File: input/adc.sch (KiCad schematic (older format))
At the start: 23 parts, among them J102 +IN, J103 -IN, U101 LTC2512-24

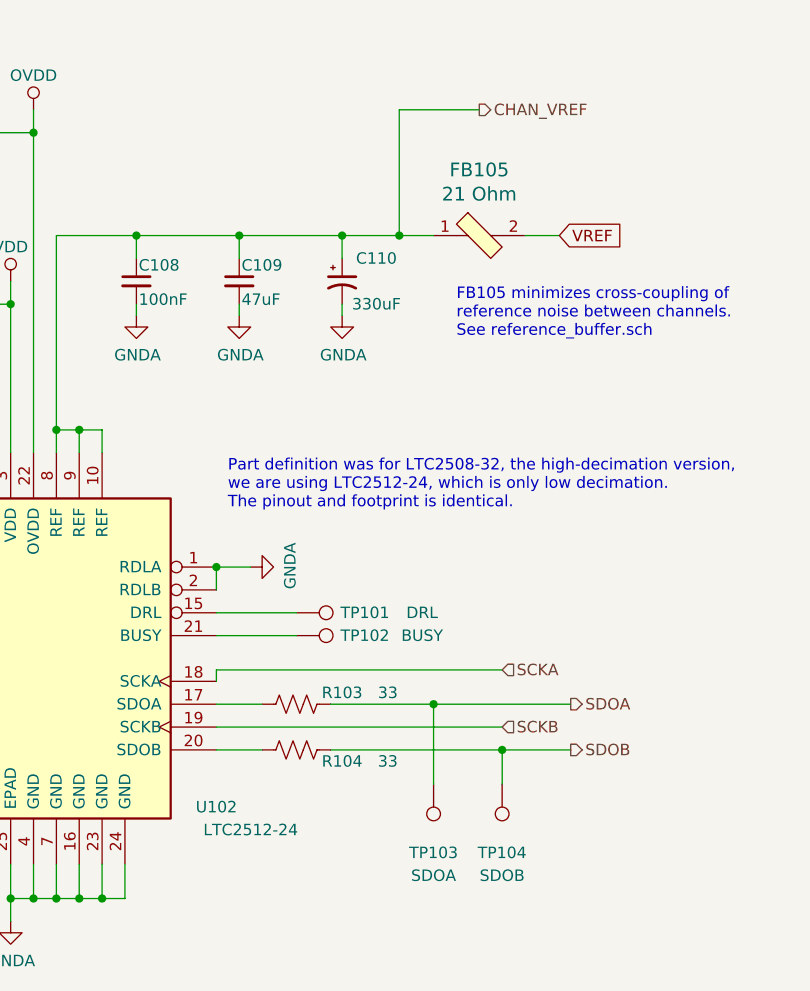
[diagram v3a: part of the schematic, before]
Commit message: Checkpoint before starting routing.  Added power and ground testpoints.
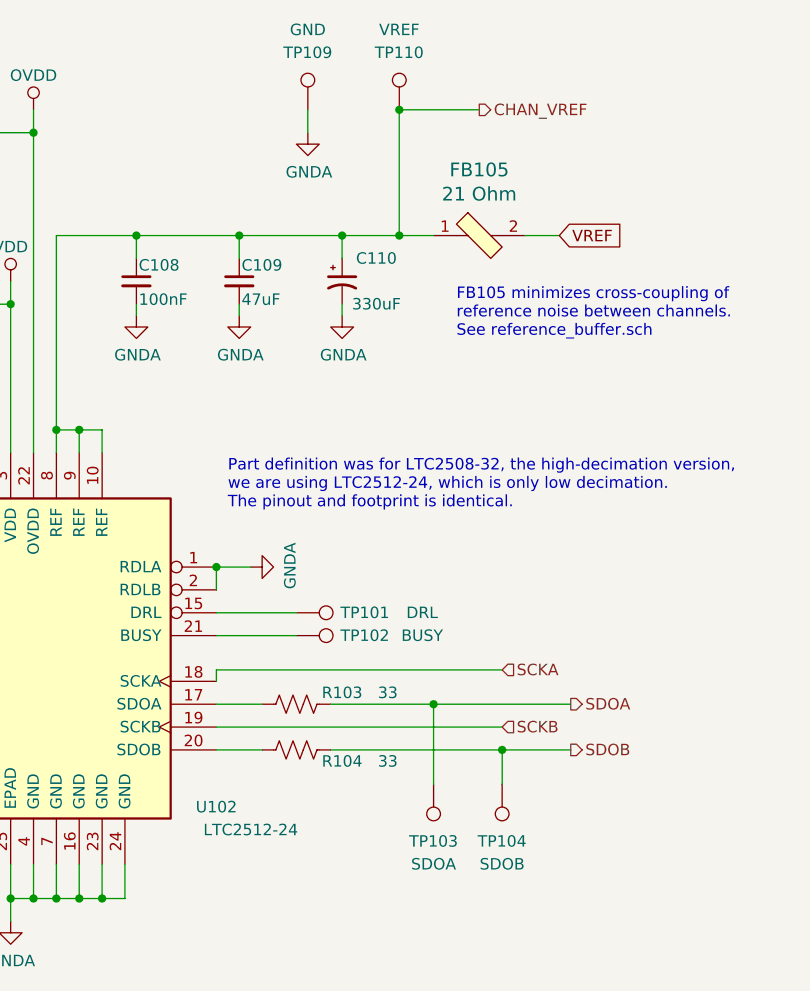
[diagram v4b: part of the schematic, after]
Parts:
- added TP109: GND, TestPoint:TestPoint_THTPad_D1.5mm_Drill0.7mm, symbol Connector:TestPoint
- added TP110: VREF, TestPoint:TestPoint_THTPad_D1.5mm_Drill0.7mm, symbol Connector:TestPoint
- C102, C103: DK line (none) -> 46; Description (none) -> 6800pF ±5% 50V Ceramic Capacitor C0G, NP0 0805 (2012 Metric); Digikey (none) -> 445-7515-1-ND
- C104, C105: DK line (none) -> 29
- C106, C107, C108: DK line (none) -> 2; Description (none) -> CAP CER 0.1UF 25V X7R 0603; Digikey (none) -> 311-1341-1-ND
- C109: DK line (none) -> 28
- C110: DK line (none) -> 19
- FB105: DK line (none) -> 24
- J102, J103: DK line (none) -> 35
- R101, R102: DK line (none) -> 9; Description (none) -> RES SMD 10 OHM 5% 1/2W 0805
- R103, R104: DK line (none) -> 52; Digikey (none) -> RMCF0603FT33R0CT-ND
- U101: DK line (none) -> 3
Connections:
- net CHAN_VREF: now also TP110.1
- net GNDA: now also TP109.1
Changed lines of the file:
@@
 EESchema Schematic File Version 4
-LIBS:input_board-cache
-EELAYER 29 0
+EELAYER 30 0
 EELAYER END
 $Descr A4 11693 8268
@@
 F 2 "Package_DFN_QFN:DFN-24-1EP_4x7mm_P0.5mm_EP2.64x6.44mm" H 5950 3050 50  0001 L CNN
 F 3 "" H 7100 2950 50  0001 C CNN
+F 4 "3" H 6900 4000 50  0001 C CNN "DK line"
 	1    6900 4000
 	1    0    0    -1
@@
 F 5 "399-5516-1-ND" H 7700 2350 50  0001 C CNN "Digikey"
 F 6 "C1210C476M9RACTU" H 7700 2350 50  0001 C CNN "MPN"
+F 7 "28" H 7700 2350 50  0001 C CNN "DK line"
 	1    7700 2350
 	1    0    0    -1
@@
 F 5 "478-5318-1-ND" H 5900 2650 50  0001 C CNN "Digikey"
 F 6 "06036D106MAT2A" H 5900 2650 50  0001 C CNN "MPN"
+F 7 "29" H 5900 2650 50  0001 C CNN "DK line"
 	1    5900 2650
 	1    0    0    -1
@@
 F 2 "Capacitor_SMD:C_0603_1608Metric" H 6250 2650 50  0001 C CNN
 F 3 "~" H 6250 2650 50  0001 C CNN
+F 4 "CAP CER 0.1UF 25V X7R 0603" H 6250 2650 50  0001 C CNN "Description"
+F 5 "311-1341-1-ND" H 6250 2650 50  0001 C CNN "Digikey"
+F 6 "2" H 6250 2650 50  0001 C CNN "DK line"
 	1    6250 2650
 	1    0    0    -1
@@
 F 5 "478-5318-1-ND" H 5900 1900 50  0001 C CNN "Digikey"
 F 6 "06036D106MAT2A" H 5900 1900 50  0001 C CNN "MPN"
+F 7 "29" H 5900 1900 50  0001 C CNN "DK line"
 	1    5900 1900
 	1    0    0    -1
@@
 F 2 "Capacitor_SMD:C_0603_1608Metric" H 6250 1900 50  0001 C CNN
 F 3 "~" H 6250 1900 50  0001 C CNN
+F 4 "CAP CER 0.1UF 25V X7R 0603" H 6250 1900 50  0001 C CNN "Description"
+F 5 "311-1341-1-ND" H 6250 1900 50  0001 C CNN "Digikey"
+F 6 "2" H 6250 1900 50  0001 C CNN "DK line"
 	1    6250 1900
 	1    0    0    -1
@@
 F 2 "Capacitor_SMD:C_0603_1608Metric" H 7250 2350 50  0001 C CNN
 F 3 "~" H 7250 2350 50  0001 C CNN
+F 4 "CAP CER 0.1UF 25V X7R 0603" H 7250 2350 50  0001 C CNN "Description"
+F 5 "311-1341-1-ND" H 7250 2350 50  0001 C CNN "Digikey"
+F 6 "2" H 7250 2350 50  0001 C CNN "DK line"
 	1    7250 2350
 	1    0    0    -1
@@
 F 2 "Capacitor_SMD:C_0805_2012Metric" H 4100 2850 50  0001 C CNN
 F 3 "~" H 4100 2850 50  0001 C CNN
+F 4 "6800pF ±5% 50V Ceramic Capacitor C0G, NP0 0805 (2012 Metric)" H 4100 2850 50  0001 C CNN "Description"
+F 5 "445-7515-1-ND" H 4100 2850 50  0001 C CNN "Digikey"
+F 6 "46" H 4100 2850 50  0001 C CNN "DK line"
 	1    4100 2850
 	1    0    0    -1
@@
 F 2 "Capacitor_SMD:C_0805_2012Metric" H 4100 3500 50  0001 C CNN
 F 3 "~" H 4100 3500 50  0001 C CNN
+F 4 "6800pF ±5% 50V Ceramic Capacitor C0G, NP0 0805 (2012 Metric)" H 4100 3500 50  0001 C CNN "Description"
+F 5 "445-7515-1-ND" H 4100 3500 50  0001 C CNN "Digikey"
+F 6 "46" H 4100 3500 50  0001 C CNN "DK line"
 	1    4100 3500
 	1    0    0    -1
@@
 F 1 "10" V 3250 2650 50  0000 C CNN
 F 2 "Resistor_SMD:R_0805_2012Metric" V 3390 2640 50  0001 C CNN
-F 3 "~" H 3350 2650 50  0001 C CNN
+F 3 "http://www.vishay.com/docs/20043/crcwhpe3.pdf" H 3350 2650 50  0001 C CNN
 F 4 "541-10TACT-ND" H 3350 2650 50  0001 C CNN "Digikey"
 F 5 "CRCW080510R0JNEAHP" H 3350 2650 50  0001 C CNN "MPN"
 F 6 "Thick film surge resist" H 3350 2650 50  0001 C CNN "Notes"
+F 7 "9" H 3350 2650 50  0001 C CNN "DK line"
+F 8 "RES SMD 10 OHM 5% 1/2W 0805" H 3350 2650 50  0001 C CNN "Description"
 	1    3350 2650
 	0    1    1    0
@@
 F 1 "10" V 3250 3700 50  0000 C CNN
 F 2 "Resistor_SMD:R_0805_2012Metric" V 3390 3690 50  0001 C CNN
-F 3 "~" H 3350 3700 50  0001 C CNN
+F 3 "http://www.vishay.com/docs/20043/crcwhpe3.pdf" H 3350 3700 50  0001 C CNN
 F 4 "541-10TACT-ND" H 3350 3700 50  0001 C CNN "Digikey"
 F 5 "CRCW080510R0JNEAHP" H 3350 3700 50  0001 C CNN "MPN"
 F 6 "Thick film surge resist" H 3350 3700 50  0001 C CNN "Notes"
+F 7 "9" H 3350 3700 50  0001 C CNN "DK line"
+F 8 "RES SMD 10 OHM 5% 1/2W 0805" H 3350 3700 50  0001 C CNN "Description"
 	1    3350 3700
 	0    1    1    0
@@
 F 2 "Resistor_SMD:R_0603_1608Metric" V 7990 4390 50  0001 C CNN
 F 3 "~" H 7950 4400 50  0001 C CNN
+F 4 "RMCF0603FT33R0CT-ND" H 7950 4400 50  0001 C CNN "Digikey"
+F 5 "52" H 7950 4400 50  0001 C CNN "DK line"
 	1    7950 4400
 	0    1    1    0
@@
 F 2 "Resistor_SMD:R_0603_1608Metric" V 7990 4190 50  0001 C CNN
 F 3 "~" H 7950 4200 50  0001 C CNN
+F 4 "RMCF0603FT33R0CT-ND" H 7950 4200 50  0001 C CNN "Digikey"
+F 5 "52" H 7950 4200 50  0001 C CNN "DK line"
 	1    7950 4200
 	0    1    1    0
@@
 F 6 "FERRITE BEAD 21 OHM 0805, 100 nH, 5 mOhm" H 8950 3150 60  0001 L CNN "Description"
 F 7 "587-1765-1-ND" H 8750 2150 50  0001 C CNN "Digikey"
+F 8 "24" H 8750 2150 50  0001 C CNN "DK line"
 	1    8750 2150
 	1    0    0    -1
@@
 F 1 "330uF" H 8300 2250 50  0000 C CNN
 F 2 "Capacitor_SMD:CP_Elec_8x6.7" H 8150 2350 50  0001 C CNN
-F 3 "~" H 8150 2350 50  0001 C CNN
+F 3 "http://www.chemi-con.co.jp/cgi-bin/CAT_DB/SEARCH/cat_db_al.cgi?e=e&j=p&pdfname=pxg" H 8150 2350 50  0001 C CNN
 F 4 "16V aluminum solid polymer, ESR 22 mOhm" H 8150 2350 50  0001 C CNN "Description"
 F 5 "565-4285-1-ND" H 8150 2350 50  0001 C CNN "Digikey"
 F 6 "APXG160ARA331MH70G" H 8150 2350 50  0001 C CNN "MPN"
+F 7 "19" H 8150 2350 50  0001 C CNN "DK line"
 	1    8150 2350
 	1    0    0    -1
@@
 AR Path="/5DFCF14D/5DA78AA2/5E4700B3" Ref="TP103"  Part="1"
 AR Path="/5DFCF14D/5E295469/5E4700B3" Ref="TP?"  Part="1"
-F 0 "TP103" H 8550 4850 50  0000 C CNN
-F 1 "SDOA" H 8550 4950 50  0000 C CNN
+F 0 "TP103" H 8550 4800 50  0000 C CNN
+F 1 "SDOA" H 8550 4900 50  0000 C CNN
 F 2 "TestPoint:TestPoint_THTPad_D1.5mm_Drill0.7mm" H 8750 4550 50  0001 C CNN
 F 3 "~" H 8750 4550 50  0001 C CNN
@@
 AR Path="/5DFCF14D/5DA78AA2/5E4705E0" Ref="TP104"  Part="1"
 AR Path="/5DFCF14D/5E295469/5E4705E0" Ref="TP?"  Part="1"
-F 0 "TP104" H 8850 4850 50  0000 C CNN
-F 1 "SDOB" H 8850 4950 50  0000 C CNN
+F 0 "TP104" H 8850 4800 50  0000 C CNN
+F 1 "SDOB" H 8850 4900 50  0000 C CNN
 F 2 "TestPoint:TestPoint_THTPad_D1.5mm_Drill0.7mm" H 9050 4550 50  0001 C CNN
 F 3 "~" H 9050 4550 50  0001 C CNN
@@
 F 2 "Connector_Coaxial:MMCX_Molex_73415-1471_Vertical" H 4850 2150 50  0001 C CNN
 F 3 " ~" H 4850 2150 50  0001 C CNN
+F 4 "35" H 4850 2150 50  0001 C CNN "DK line"
 	1    4850 2150
 	1    0    0    -1
@@
 F 2 "Connector_Coaxial:MMCX_Molex_73415-1471_Vertical" H 4850 4150 50  0001 C CNN
 F 3 " ~" H 4850 4150 50  0001 C CNN
+F 4 "35" H 4850 4150 50  0001 C CNN "DK line"
 	1    4850 4150
 	1    0    0    -1
@@
 F 1 "GND lift" V 5000 4600 50  0000 C CNN
 F 2 "Resistor_SMD:R_0603_1608Metric" V 5140 4590 50  0001 C CNN
-F 3 "http://www.vishay.com/docs/28758/tnpw_e3.pdf" H 5100 4600 50  0001 C CNN
+F 3 "" H 5100 4600 50  0001 C CNN
 	1    5100 4600
 	-1   0    0    1
@@
 Wire Wire Line
 	5100 4350 5100 4450
+$Comp
+L Connector:TestPoint TP110
+U 1 1 5E39D8AC
+P 8400 1600
+AR Path="/5DFCF14D/5DA78AA2/5E39D8AC" Ref="TP110"  Part="1"
+AR Path="/5DFCF14D/5E295469/5E39D8AC" Ref="TP?"  Part="1"
+F 0 "TP110" H 8400 1850 50  0000 C CNN
+F 1 "VREF" H 8400 1950 50  0000 C CNN
+F 2 "TestPoint:TestPoint_THTPad_D1.5mm_Drill0.7mm" H 8600 1600 50  0001 C CNN
+F 3 "~" H 8600 1600 50  0001 C CNN
+	1    8400 1600
+	1    0    0    -1
+$EndComp
+Connection ~ 8400 1600
+$Comp
+L Connector:TestPoint TP109
+U 1 1 5E3A02ED
+P 8000 1600
+AR Path="/5DFCF14D/5DA78AA2/5E3A02ED" Ref="TP109"  Part="1"
+AR Path="/5DFCF14D/5E295469/5E3A02ED" Ref="TP?"  Part="1"
+F 0 "TP109" H 8000 1850 50  0000 C CNN
+F 1 "GND" H 8000 1950 50  0000 C CNN
+F 2 "TestPoint:TestPoint_THTPad_D1.5mm_Drill0.7mm" H 8200 1600 50  0001 C CNN
+F 3 "~" H 8200 1600 50  0001 C CNN
+	1    8000 1600
+	1    0    0    -1
+$EndComp
+$Comp
+L power:GNDA #PWR?
+U 1 1 5E3A05B0
+P 8000 1700
+AR Path="/5E3A05B0" Ref="#PWR?"  Part="1"
+AR Path="/5DA78AA2/5E3A05B0" Ref="#PWR?"  Part="1"
+AR Path="/5DFCF14D/5DA78AA2/5E3A05B0" Ref="#PWR0164"  Part="1"
+AR Path="/5DFCF14D/5E295469/5E3A05B0" Ref="#PWR?"  Part="1"
+F 0 "#PWR0164" H 8000 1450 50  0001 C CNN
+F 1 "GNDA" H 8005 1527 50  0000 C CNN
+F 2 "" H 8000 1700 50  0001 C CNN
+F 3 "" H 8000 1700 50  0001 C CNN
+	1    8000 1700
+	1    0    0    -1
+$EndComp
+Wire Wire Line
+	8000 1700 8000 1600
 $EndSCHEMATC

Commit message: Lots of work on routing input_board.kicad_pcb, not done yet.
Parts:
- removed TP104: SDOB, TestPoint:TestPoint_THTPad_D1.5mm_Drill0.7mm, symbol Connector:TestPoint
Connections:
- net DRL: now reaches TP101.1, U101.15 (DRL)
- net BUSY: now reaches TP102.1, U101.21 (BUSY)
- net J102_J103_GND: now reaches J102.2 (Ext), J103.2 (Ext), R133.2
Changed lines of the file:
@@
-	-1   0    0    1
-$EndComp
-$Comp
-L Connector:TestPoint TP104
-U 1 1 5E4705E0
-P 8850 4550
-AR Path="/5DFCF14D/5DA78AA2/5E4705E0" Ref="TP104"  Part="1"
-AR Path="/5DFCF14D/5E295469/5E4705E0" Ref="TP?"  Part="1"
-F 0 "TP104" H 8850 4800 50  0000 C CNN
-F 1 "SDOB" H 8850 4900 50  0000 C CNN
-F 2 "TestPoint:TestPoint_THTPad_D1.5mm_Drill0.7mm" H 9050 4550 50  0001 C CNN
-F 3 "~" H 9050 4550 50  0001 C CNN
-	1    8850 4550
 	-1   0    0    1
 $EndComp
@@
 Wire Wire Line
 	8550 4200 9150 4200
-Wire Wire Line
-	8850 4550 8850 4400
-Connection ~ 8850 4400
-Wire Wire Line
-	8850 4400 9150 4400
-Wire Wire Line
-	8100 4400 8850 4400
 $Comp
 L Connector:Conn_Coaxial J?
@@
 Wire Wire Line
 	8000 1700 8000 1600
+Text Label 7725 3800 0    50   ~ 0
+DRL
+Text Label 7725 3900 0    50   ~ 0
+BUSY
+Wire Wire Line
+	8100 4400 9150 4400
+Text Label 4975 2350 0    50   ~ 0
+J102_J103_GND
 $EndSCHEMATC

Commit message: Input board is nearly ready to send off for the first spin.
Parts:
- U101: footprint Package_DFN_QFN:DFN-24-1EP_4x7mm_P0.5mm_EP2.64x6.44mm -> input:DFN-24-1EP_4x7mm_P0.5mm_EP2.64x6.44mm

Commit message: Various tweaks to schematic which help in the PCB view, mainly getting informative net names. Also unscrambled the + and - paths in the input channel.  This avoided a cross-over before the first stage, and an unintended inversion, but mostly just made net naming less confusing.
Getting better net names made it easier to review the PCB to see if it made sense.  I checked
the ICs on the PCB against the datasheet pinout, and while doing this fixed an actual bug where
I had BIST-+ and BIST+-swapped.

I made some tweaks on the PCB to try to equalize the copper area on the input nets so as to
match the capacitance.  I tweaked the top-side ground pours somewhat, adding in the regulator
area, removing around the high speed traces.

Some changes from gerber viewing.  I reduced the solder mask clearances so that we get mask
web between the SOIC and DFN pads.  I reduced the pad size of the big via from 1.2 to 1.0 mm.
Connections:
- net ADC_IN-: now reaches C101.2, C103.2, J103.1 (In), R102.1, U101.6 (IN-)
- net ADC_IN+: now reaches C101.1, C102.1, J102.1 (In), R101.1, U101.5 (IN+)
- net +in renamed +IN_ADC
- net -in renamed -IN_ADC
